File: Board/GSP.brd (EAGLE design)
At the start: 85.1 x 61.9 mm, 3 parts

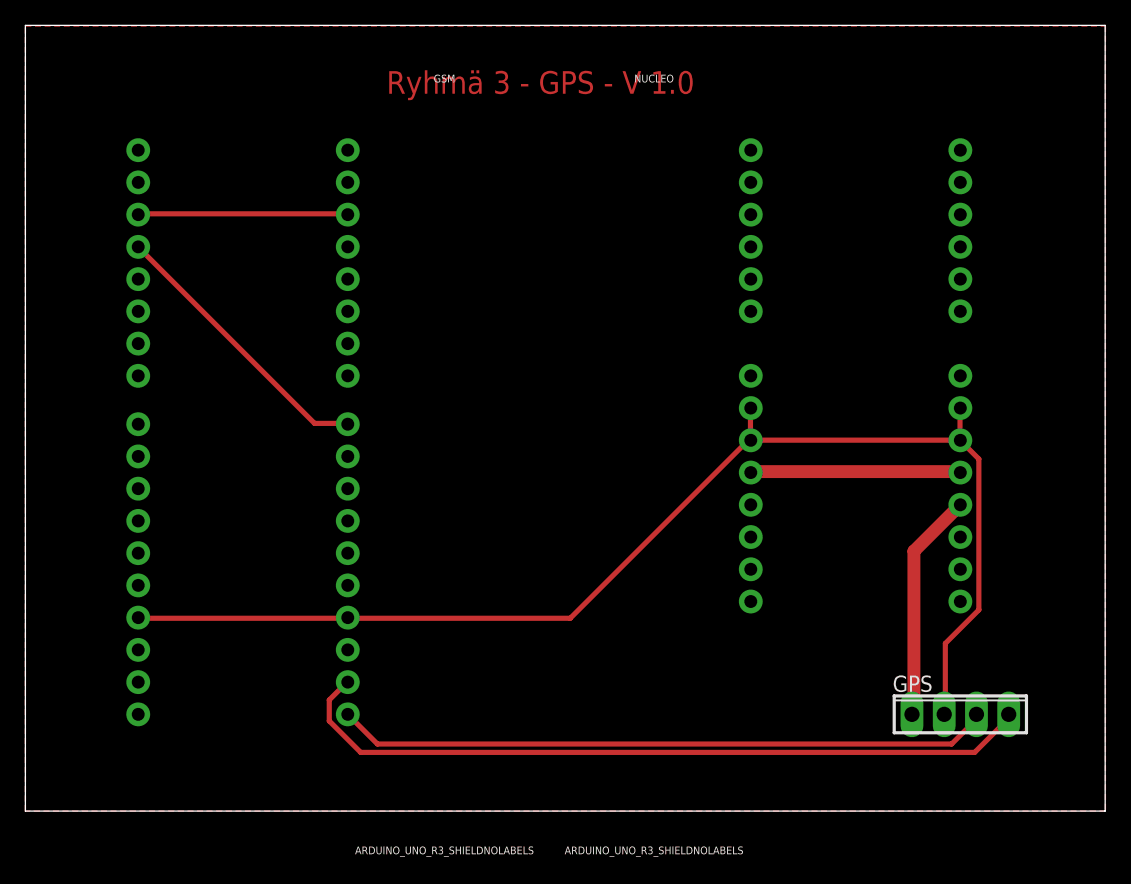
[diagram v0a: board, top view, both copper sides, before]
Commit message: Updated board. Test of webpage.
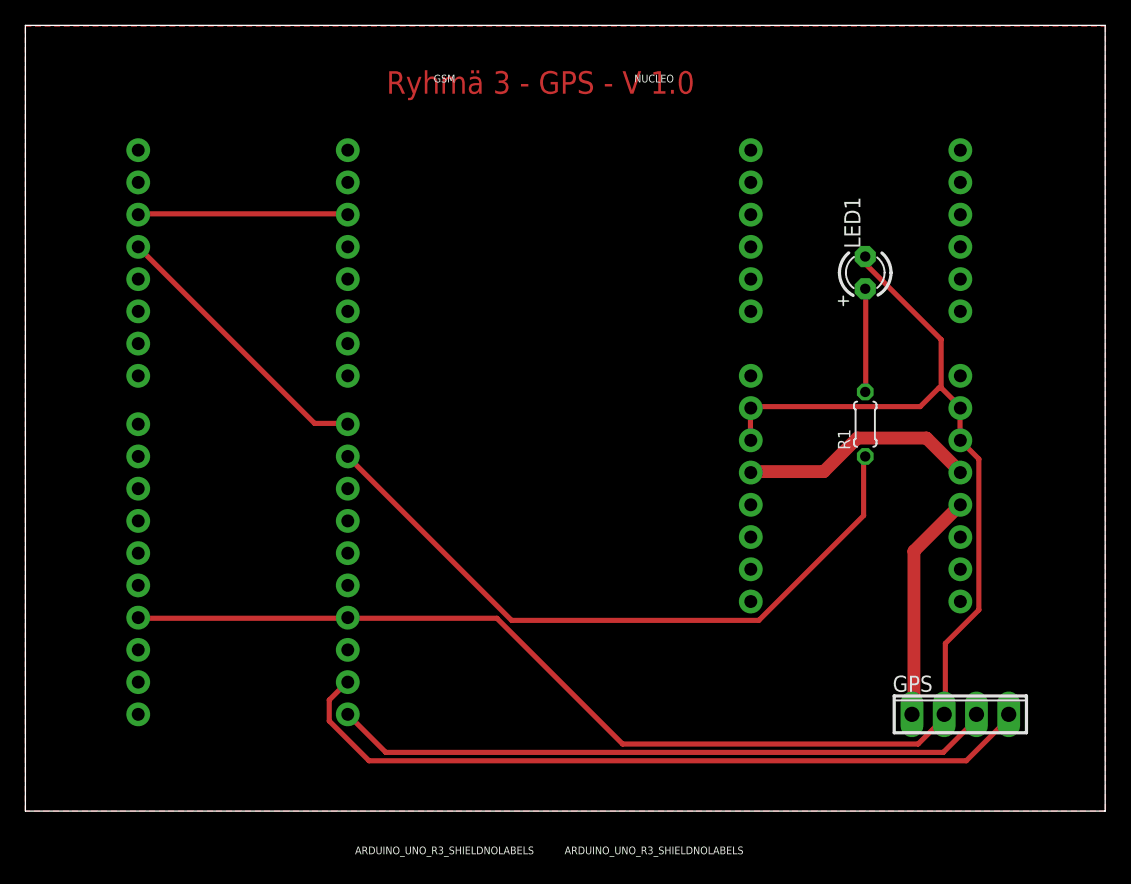
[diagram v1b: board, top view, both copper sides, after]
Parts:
- added LED1: led, adafruit:LED3MM
- added R1: 200 Ohm, rcl:0204/5
- GPS: value (none) -> GPS pins
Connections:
- new net N$2: NUCLEO.D9, R1.1
- new net N$3: LED1.A, R1.2
- net GND: now also LED1.K
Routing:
- net N$2: track 0.00 -> 54.2 mm
- net GND: track 99.1 -> 127.8 mm
- net N$3: track 0.00 -> 8.18 mm
- net N$1: track 16.6 -> 18.8 mm
- net N$7: track 59.7 -> 60.2 mm
- net N$8: track 51.7 -> 52.3 mm
